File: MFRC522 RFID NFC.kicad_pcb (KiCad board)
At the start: 2 copper layers, 27 parts, among them U1 MFRC522/RC522

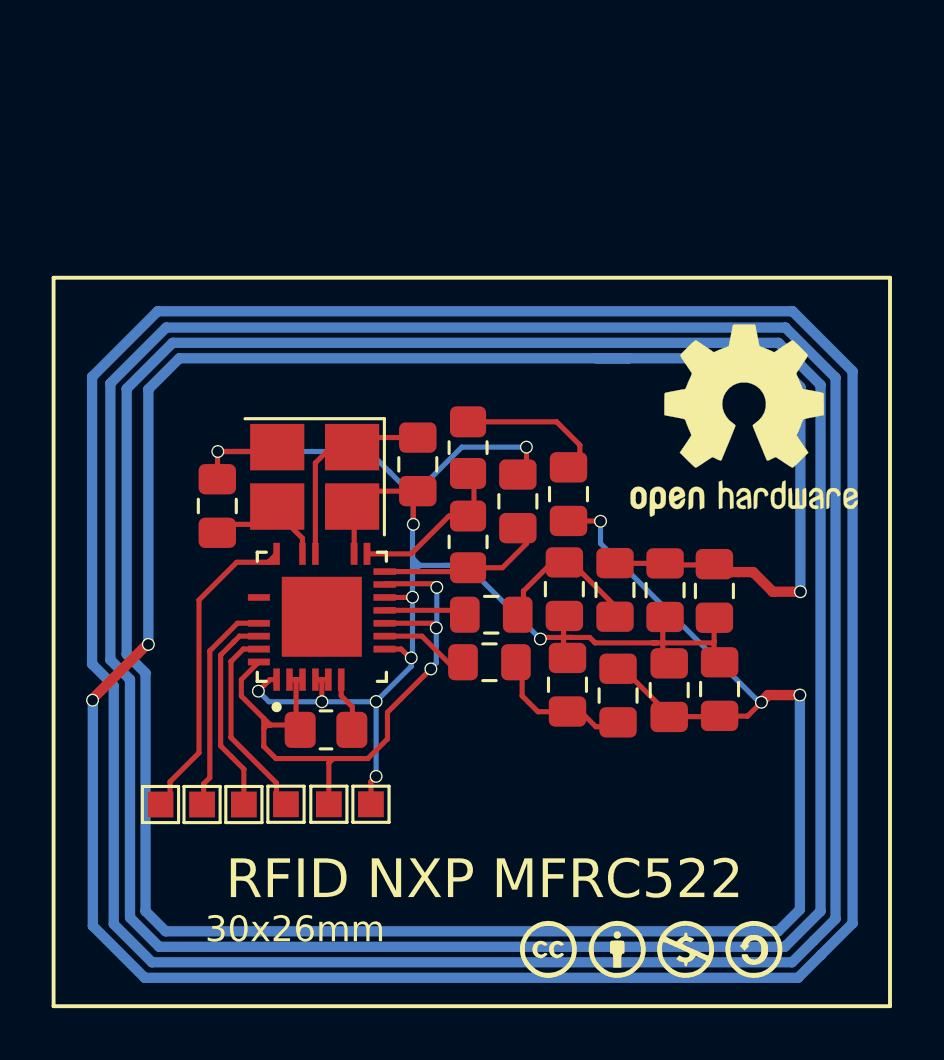
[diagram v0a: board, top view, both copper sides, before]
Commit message: rev. 1.1
added missing components
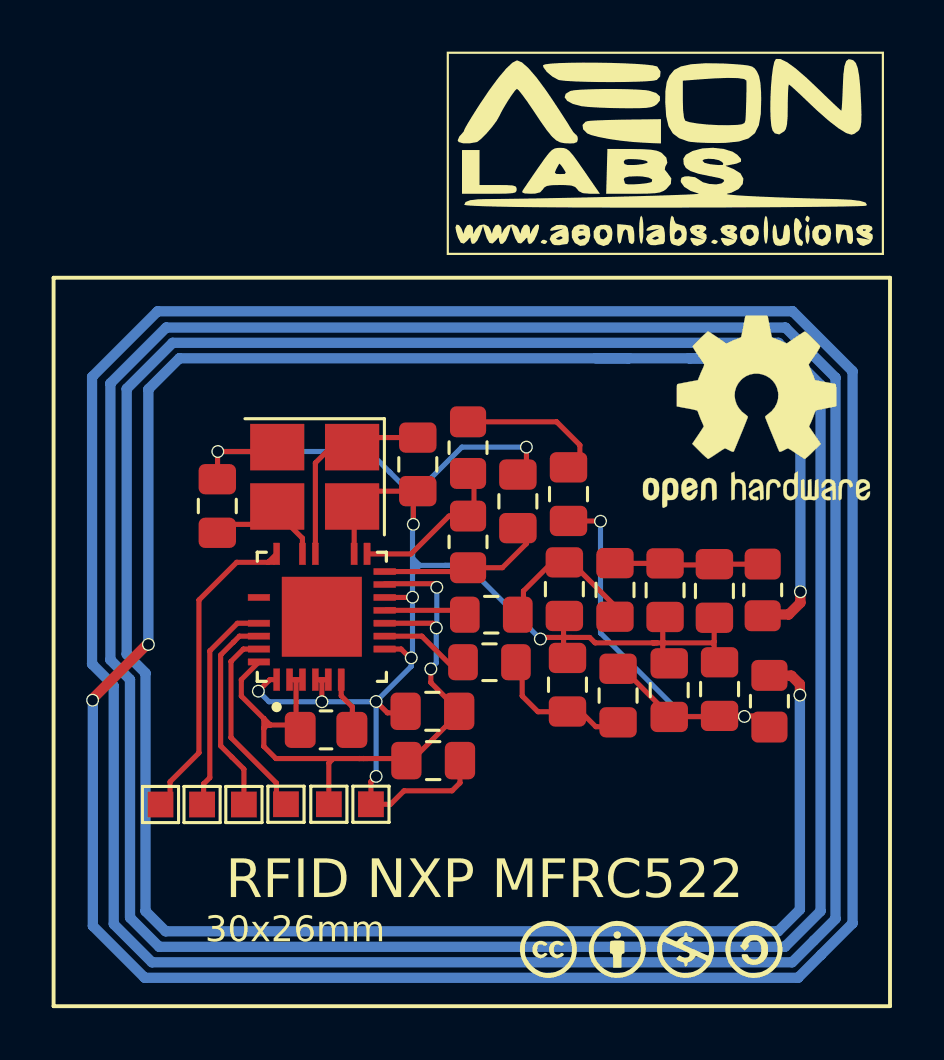
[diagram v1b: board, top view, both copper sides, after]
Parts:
- added 300R1: NR18, Resistor_SMD:R_0805_2012Metric_Pad1.20x1.40mm_HandSolder, F.Cu at (133.5, 111.4)
- added 300R2: NR17, Resistor_SMD:R_0805_2012Metric_Pad1.20x1.40mm_HandSolder, F.Cu at (133.8, 115.7)
- added G***: LOGO, AeonLabs Logosy:aeon logo www, F.Cu at (129.7, 94.4)
- added NC26: 100nF, Capacitor_SMD:C_0805_2012Metric_Pad1.18x1.45mm_HandSolder, F.Cu at (120.7, 116.1)
- added NC27: 100nF, Capacitor_SMD:C_0805_2012Metric_Pad1.18x1.45mm_HandSolder, F.Cu at (120.7, 118.0)
- NC5, NC6: value 104???? -> 100nF
- moved REF** 0.59 mm to (133.3, 104.5)
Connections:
- net ANT_GND renamed GND
- net ANT_TX1 renamed Net-(NC18-Pad2)
- net ANT_TX2 renamed Net-(NC19-Pad2)
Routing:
- net Net-(NC18-Pad2): track 418.2 -> 19.3 mm, vias 6 -> 2
- net ANT_TX1: track 0.00 -> 398.7 mm, vias 0 -> 4
- net GND: track 65.3 -> 71.3 mm
- net 3V3: track 25.9 -> 28.3 mm
- net Net-(NC19-Pad2): track 4.11 -> 5.98 mm
